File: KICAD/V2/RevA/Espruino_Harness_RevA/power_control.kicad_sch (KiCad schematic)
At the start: 41 parts, among them J1001 OPERATING_MODE, Q1 2N7002, Q1101 AO3401A, U1001 TPS2116DRL, U1002 TPS22917DBV, U1101 TPS2559-Q1, U1102 74AHCT1G125, U1103 INA226, U1104 INA228, U1105 74LVC2G08

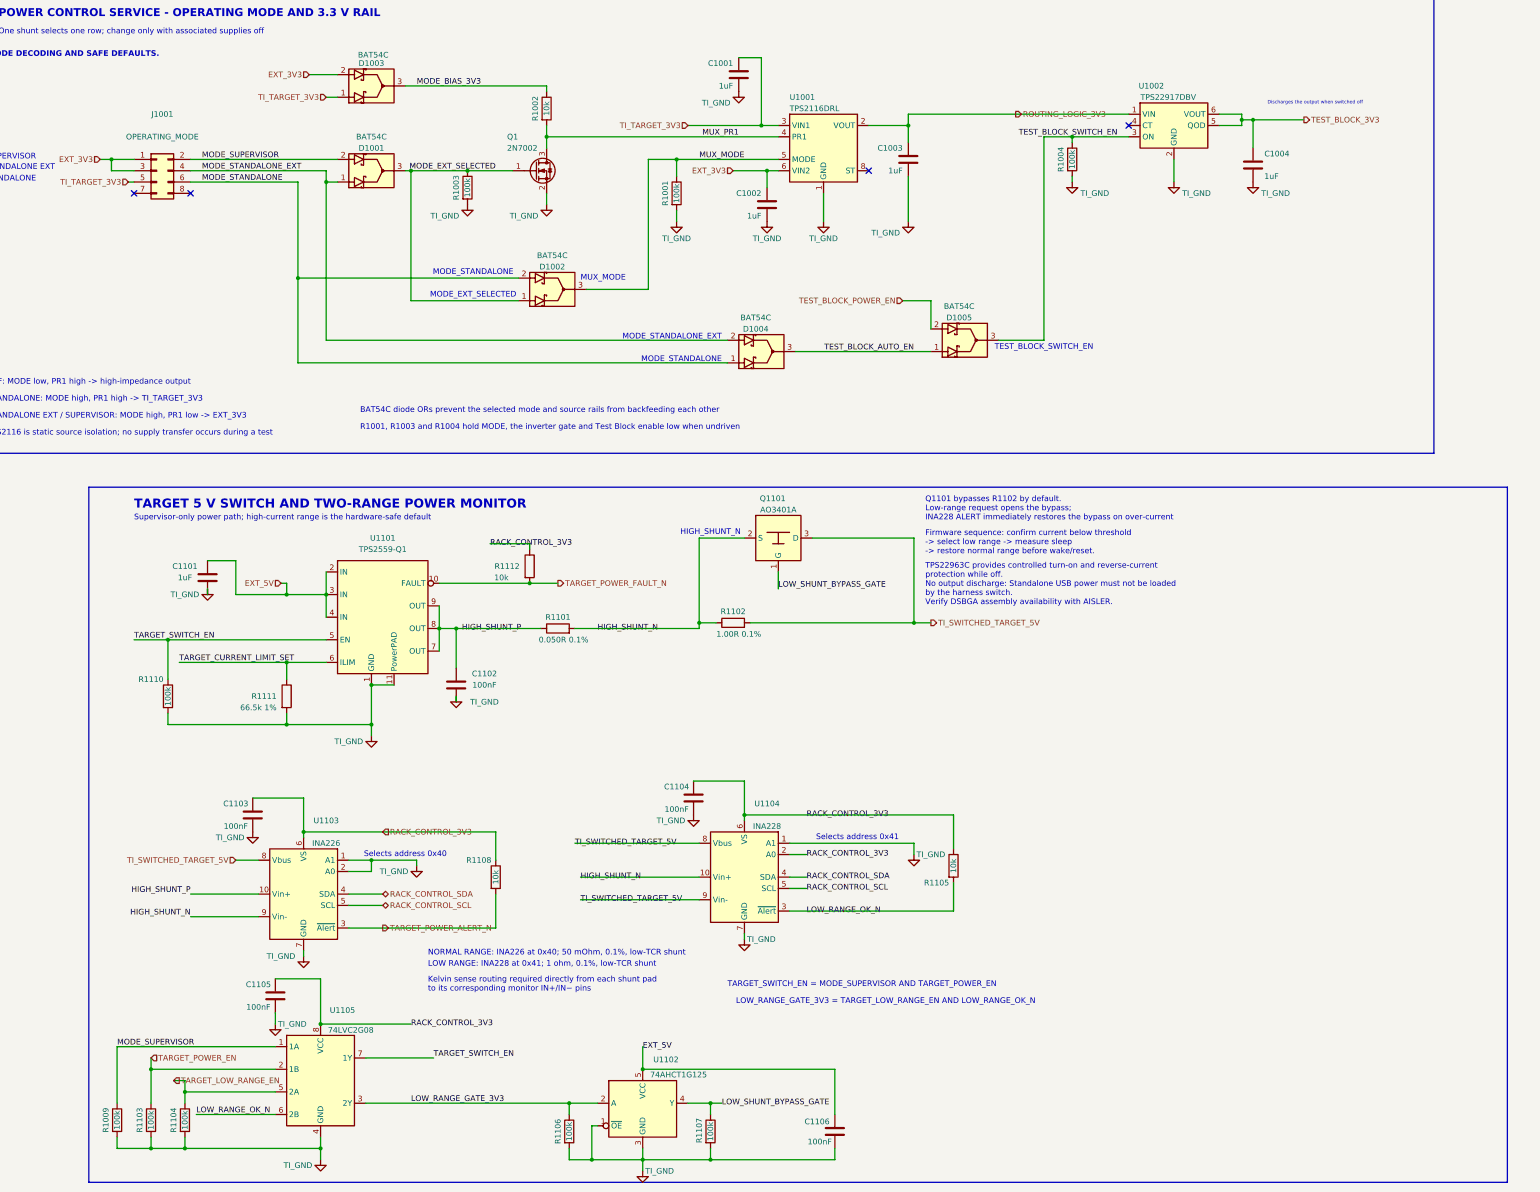
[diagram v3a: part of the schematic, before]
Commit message: Revise low-range power measurement path
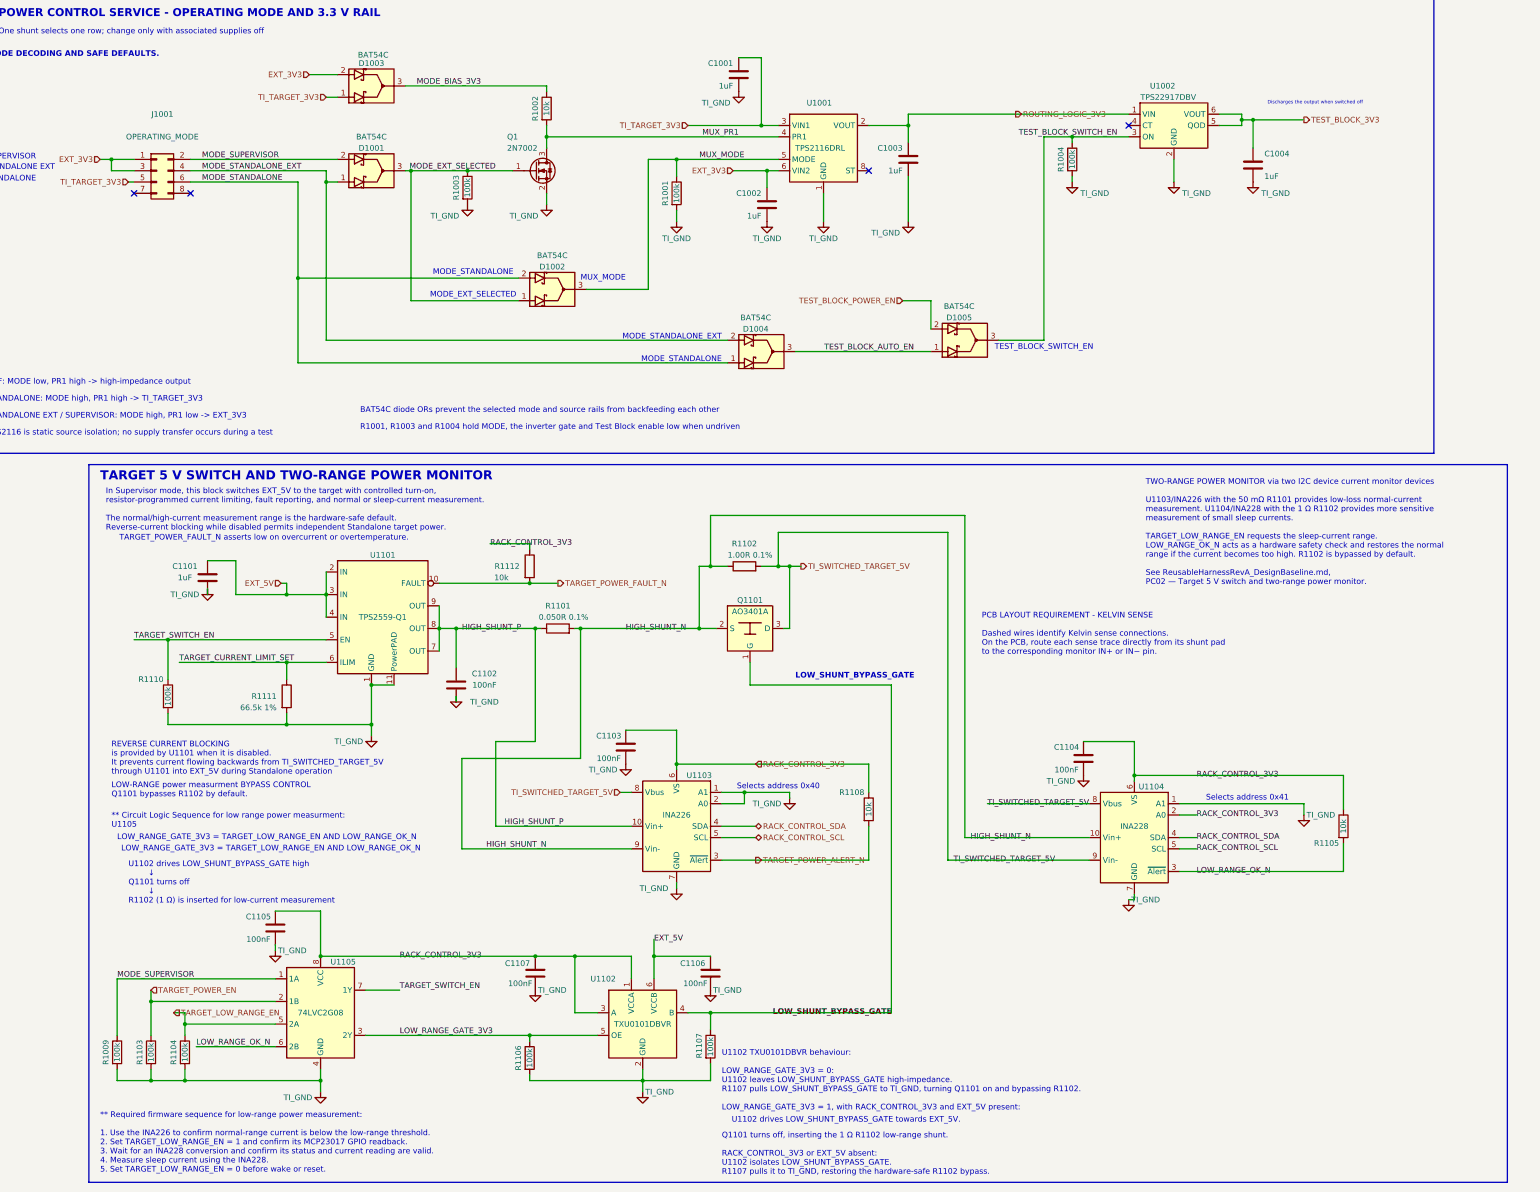
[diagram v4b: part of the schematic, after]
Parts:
- removed U1102: 74AHCT1G125, Package_TO_SOT_SMD:SOT-23-5, symbol Espruino_Harness_RevA:74AHCT1G125_RANGE_DRIVER
- added C1107: 100nF, Capacitor_SMD:C_0603_1608Metric, symbol Espruino_Harness_RevA:C
- added U1102: TXU0101DBVR, Package_TO_SOT_SMD:SOT-23-6, symbol Espruino_Harness_RevA:TXU0101_RANGE_DRIVER
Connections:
- net EXT_5V: now also U1102.6 (VCCB)
- net LOW_RANGE_GATE_3V3: now also U1102.5 (OE)
- net LOW_SHUNT_BYPASS_GATE: now also U1102.4 (B)
- net RACK_CONTROL_3V3: now also C1107.1, U1102.1 (VCCA), U1102.3 (A)
- net TI_GND: now also C1107.2, U1102.2 (GND)
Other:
- note added: "** Circuit Logic Sequence for low range power measurment: U1105"
- note added: "** Required firmware sequence for low-range power measurement: 1. Use the INA226 to confirm normal-range current is below the low-range threshold. 2. Set TARGET_LOW_RANGE_EN = 1 and confirm its MCP23017 GPIO readback. 3. Wait for an INA228 conversion and confirm its status and current reading are valid. 4. Measure sleep current using the INA228. 5. Set TARGET_LOW_RANGE_EN = 0 before wake or reset."
- note added: "In Supervisor mode, this block switches EXT_5V to the target with controlled turn-on, resistor-programmed current limiting, fault reporting, and normal or sleep-current measurement. The normal/high-current measurement range is the hardware-safe default. Reverse-current blocking while disabled permits independent Standalone target power."
- note added: "LOW-RANGE power measurment BYPASS CONTROL Q1101 bypasses R1102 by default."
- note added: "LOW_SHUNT_BYPASS_GATE"
- note added: "PCB LAYOUT REQUIREMENT - KELVIN SENSE Dashed wires identify Kelvin sense connections. On the PCB, route each sense trace directly from its shunt pad to the corresponding monitor IN+ or IN− pin."
- note added: "Q1101 turns off, inserting the 1 Ω R1102 low-range shunt. RACK_CONTROL_3V3 or EXT_5V absent: U1102 isolates LOW_SHUNT_BYPASS_GATE. R1107 pulls it to TI_GND, restoring the hardware-safe R1102 bypass."
- note added: "REVERSE CURRENT BLOCKING is provided by U1101 when it is disabled. It prevents current flowing backwards from TI_SWITCHED_TARGET_5V through U1101 into EXT_5V during Standalone operation"
- note added: "TARGET_POWER_FAULT_N asserts low on overcurrent or overtemperature."
- note added: "TWO-RANGE POWER MONITOR via two I2C device current monitor devices U1103/INA226 with the 50 mΩ R1101 provides low-loss normal-current measurement. U1104/INA228 with the 1 Ω R1102 provides more sensitive measurement of small sleep currents. TARGET_LOW_RANGE_EN requests the sleep-current range. LOW_RANGE_OK_N acts as a hardware safety check and restores the normal range if the current becomes too h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"
- note added: "U1102 TXU0101DBVR behaviour: LOW_RANGE_GATE_3V3 = 0: U1102 leaves LOW_SHUNT_BYPASS_GATE high-impedance. R1107 pulls LOW_SHUNT_BYPASS_GATE to TI_GND, turning Q1101 on and bypassing R1102. LOW_RANGE_GATE_3V3 = 1, with RACK_CONTROL_3V3 and EXT_5V present:"
- note added: "U1102 drives LOW_SHUNT_BYPASS_GATE high ↓ Q1101 turns off ↓ R1102 (1 Ω) is inserted for low-current measurement"
- note added: "U1102 drives LOW_SHUNT_BYPASS_GATE towards EXT_5V."
- note removed: "Firmware sequence: confirm current below threshold -> select low range -> measure sleep -> restore normal range before wake/reset."
- note removed: "HIGH_SHUNT_N"
- note removed: "Kelvin sense routing required directly from each shunt pad to its corresponding monitor IN+/IN− pins"
- note removed: "LOW RANGE: INA228 at 0x41; 1 ohm, 0.1%, low-TCR shunt"
- note removed: "NORMAL RANGE: INA226 at 0x40; 50 mOhm, 0.1%, low-TCR shunt"
- note removed: "Q1101 bypasses R1102 by default. Low-range request opens the bypass; INA228 ALERT immediately restores the bypass on over-current"
- note removed: "Supervisor-only power path; high-current range is the hardware-safe default"
- note removed: "TARGET_SWITCH_EN = MODE_SUPERVISOR AND TARGET_POWER_EN"
- note removed: "TPS22963C provides controlled turn-on and reverse-current protection while off. No output discharge: Standalone USB power must not be loaded by the harness switch. Verify DSBGA assembly availability with AISLER."
- moved on the sheet: C1103, C1104, C1105, C1106, Q1101, R1009, R1102, R1103, R1104, R1105, R1106, R1107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

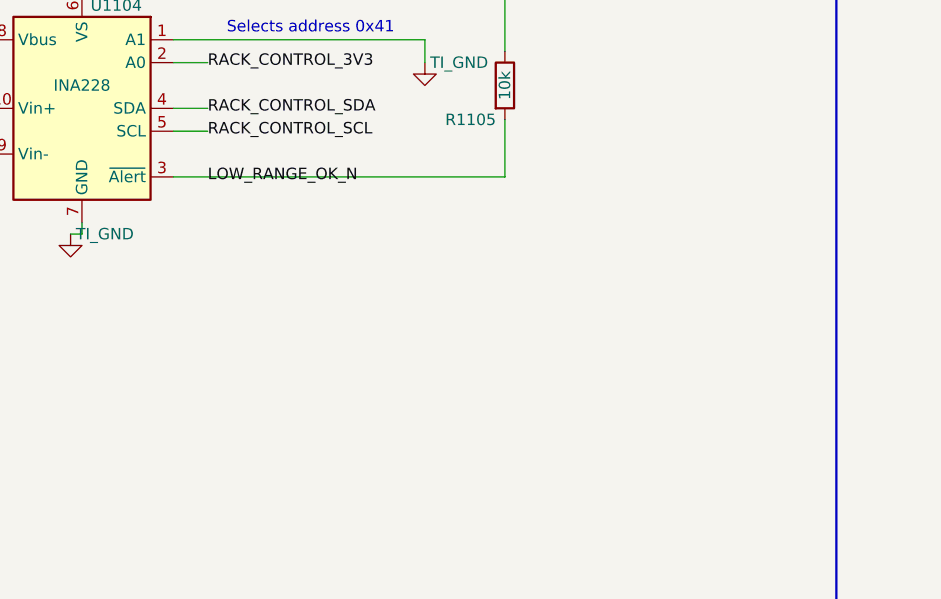
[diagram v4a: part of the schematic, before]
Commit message: Implement low-range power alert integration
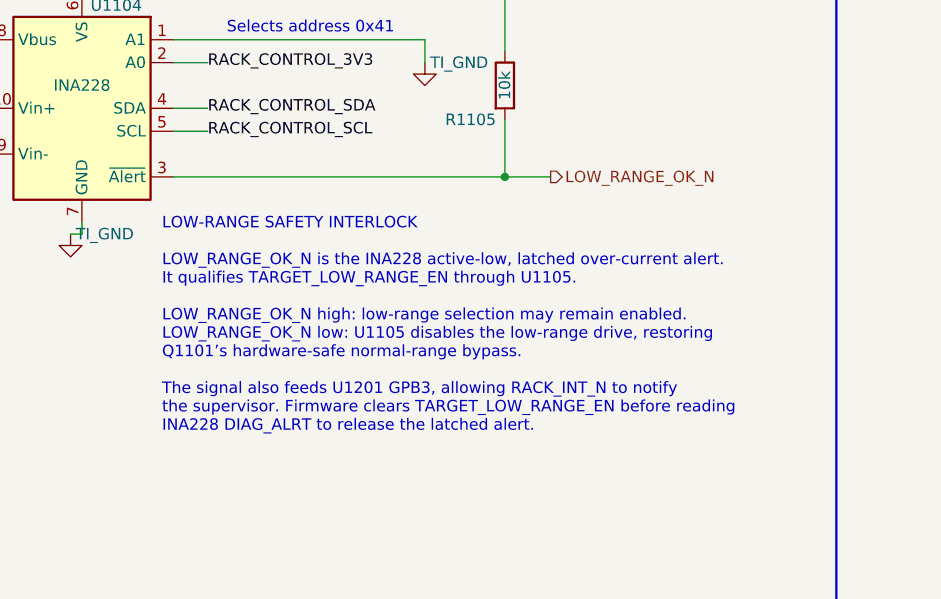
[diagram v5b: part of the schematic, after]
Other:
- note added: "LOW-RANGE SAFETY INTERLOCK LOW_RANGE_OK_N is the INA228 active-low, latched over-current alert. It qualifies TARGET_LOW_RANGE_EN through U1105. LOW_RANGE_OK_N high: low-range selection may remain enabled. LOW_RANGE_OK_N low: U1105 disables the low-range drive, restoring Q1101’s hardware-safe normal-range bypass. The signal also feeds U1201 GPB3, allowing RACK_INT_N to notify the supervisor. Firmw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"
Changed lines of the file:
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@@
 		)
 	)
+	(text "LOW-RANGE SAFETY INTERLOCK\n\nLOW_RANGE_OK_N is the INA228 active-low, latched over-current alert.\nIt qualifies TARGET_LOW_RANGE_EN through U1105.\n\nLOW_RANGE_OK_N high: low-range selection may remain enabled.\nLOW_RANGE_OK_N low: U1105 disables the low-range drive, restoring\nQ1101’s hardware-safe normal-range bypass.\n\nThe signal also feeds U1201 GPB3, allowing RACK_INT_N to notify\nthe supervisor. Firmware clears TARGET_LOW_RANGE_EN before reading\nINA228 DIAG_ALRT to release the latched alert."
+		(exclude_from_sim no)
+		(at 312.42 231.14 0)
+		(effects
+			(font
+				(size 1.27 1.27)
+			)
+			(justify left)
+		)
+	)
 	(text "One shunt selects one row; change only with associated supplies off"
 		(exclude_from_sim no)
@@
 	)
 	(junction
+		(at 350.52 214.63)
+		(diameter 0)
+		(color 0 0 0 0)
+	)
+	(junction
 		(at 168.91 160.02)
 		(diameter 0)
@@
 	(wire
 		(pts
+			(xy 355.6 214.63) (xy 350.52 214.63)
+		)
+		(stroke
+			(width 0)
+			(type default)
+		)
+	)
+	(wire
+		(pts
 			(xy 86.36 179.07) (xy 86.36 181.61)
 		)
@@
 	)
 	(label "LOW_RANGE_OK_N"
-		(at 317.5 214.63 0)
-		(effects
-			(font
-				(size 1.27 1.27)
-			)
-			(justify left)
-		)
-	)
-	(label "LOW_RANGE_OK_N"
 		(at 92.71 254 0)
 		(effects
@@
 		)
 	)
+	(hierarchical_label "LOW_RANGE_OK_N"
+		(shape output)
+		(at 355.6 214.63 0)
+		(effects
+			(font
+				(size 1.27 1.27)
+			)
+			(justify left)
+		)
+	)
 	(hierarchical_label "ROUTING_LOGIC_3V3"
 		(shape output)
@@
 			)
 		)
-		(property "Description" "TPS2116 VIN1 local input capacitor"
+		(property "Description" "TXU0101 VCCA 3.3 V decoupling"
 			(at 168.91 237.49 0)
 			(effects
@@
 			)
 		)
-		(property "Description" "TPS2116 VIN1 local input capacitor"
+		(property "Description" "TXU0101 VCCB 5 V decoupling"
 			(at 208.28 237.49 0)
 			(effects

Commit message: Refine Rev-A power control implementation
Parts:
- added C1005: 2.2 nF, Capacitor_SMD:C_0603_1608Metric, symbol Espruino_Harness_RevA:C
- D1001, D1002, D1003, D1004, D1005: value BAT54C -> BAT54C-E3-08
- J1001: value OPERATING_MODE -> OPERATING_MODE Selection
- Q1001: renamed from Q1; value 2N7002 -> DMN2024UQ-7; symbol Espruino_Harness_RevA:NMOS_2N7002_GSD -> Espruino_Harness_RevA:DMN2024UQ-7
- R1101: value 0.050R 0.1% -> 0.050R 1.0%; footprint Resistor_SMD:R_0603_1608Metric -> Espruino_Harness_RevA:R_Shunt_Yageo_PE2512_CurrentSense
- R1102: value 1.00R 0.1% -> 1.00R 1.0%; footprint Resistor_SMD:R_0603_1608Metric -> Espruino_Harness_RevA:R_Shunt_Bourns_CHP2512_CurrentSense
- U1101: footprint (none) -> Espruino_Harness_RevA:TPS2559Q1_DRC0010K_VSON10_EP
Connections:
- net ROUTING_LOGIC_3V3: now also C1005.2
- net at U1002.4 (CT): now also C1005.1
- no-connect marks 4 -> 3
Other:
- note added: "** Circuit Logic Sequence for operating mode and 3.3 V rails: D1001 MODE_EXT_SELECTED = MODE_STANDALONE_EXT OR MODE_SUPERVISOR D1002 MUX_MODE = MODE_STANDALONE OR MODE_EXT_SELECTED D1003 MODE_BIAS_3V3 = TI_TARGET_3V3 OR EXT_3V3 Diode-isolated logic bias only; it does not combine the load-power rails. Q1001 / R1002 MODE_EXT_SELECTED low -> MUX_PR1 high MODE_EXT_SELECTED high -> MUX_PR1 low U1001 s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"
- note added: "C0G/NP0, ±10% or better 10 V minimum,"
- note added: "J1001 OFF: MODE low, PR1 high -> high-impedance output STANDALONE: MODE high, PR1 high -> TI_TARGET_3V3 STANDALONE EXT / SUPERVISOR: MODE high, PR1 low -> EXT_3V3 Change the Operating Mode shunt only with both 3.3 V sources off."
- note added: "KELVIN SENSE"
- note added: "Selects which 3.3 V source supplies ROUTING_LOGIC_3V3. Determines if that rail is passed on to TEST_BLOCK_3V3."
- note added: "TPS2116 Power Mux with Manual and Priority Switchover"
- note added: "TPS2116 provides static source isolation; no supply transfer occurs during a test."
- note added: "TPS22917 Ultra-Low Leakage Load Switch"
- note added: "TPS22917DBV Active-high Test Block 3.3 V load switch. C1005 controls turn-on slew and inrush current. QOD discharges TEST_BLOCK_3V3 when disabled. No current limiting or overload protection."
- note added: "| Device| OR inputs | Output | | |-------|---------------------------------------------|------------------------|-----------------------------------------------------------------------------------| | D1001 | MODE_STANDALONE_EXT , MODE_SUPERVISOR | MODE_EXT_SELECTED | Indicates that U1001 must use the external 3.3 V supply. | | D1002 | MODE_STANDALONE , MODE_EXT_SELECTED | MUX_MODE | Enables U1001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"
- note added: "| Device| OR inputs | Output | | |-------|---------------------------------------------|------------------------|-----------------------------------------------------------------------------------| | D1001 | `MODE_STANDALONE_EXT`, `MODE_SUPERVISOR` | `MODE_EXT_SELECTED` | Indicates that U1001 must use the external 3.3 V supply. | | D1002 | `MODE_STANDALONE`, `MODE_EXT_SELECTED` | `MUX_MODE` | Ena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"
- note removed: "Discharges the output when switched off"
- note removed: "MODE DECODING AND SAFE DEFAULTS."
- note removed: "OFF: MODE low, PR1 high -> high-impedance output"
- note removed: "One shunt selects one row; change only with associated supplies off"
- note removed: "STANDALONE EXT / SUPERVISOR: MODE high, PR1 low -> EXT_3V3"
- note removed: "STANDALONE: MODE high, PR1 high -> TI_TARGET_3V3"
- note removed: "TPS2116 is static source isolation; no supply transfer occurs during a test"
- moved on the sheet: C1001, C1002, C1003, C1004, D1001, D1002, D1003, D1004, D1005, J1001, Q1001, R1001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
